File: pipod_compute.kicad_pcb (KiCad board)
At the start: 2 copper layers, 55.5 x 84.8 mm, 2 parts

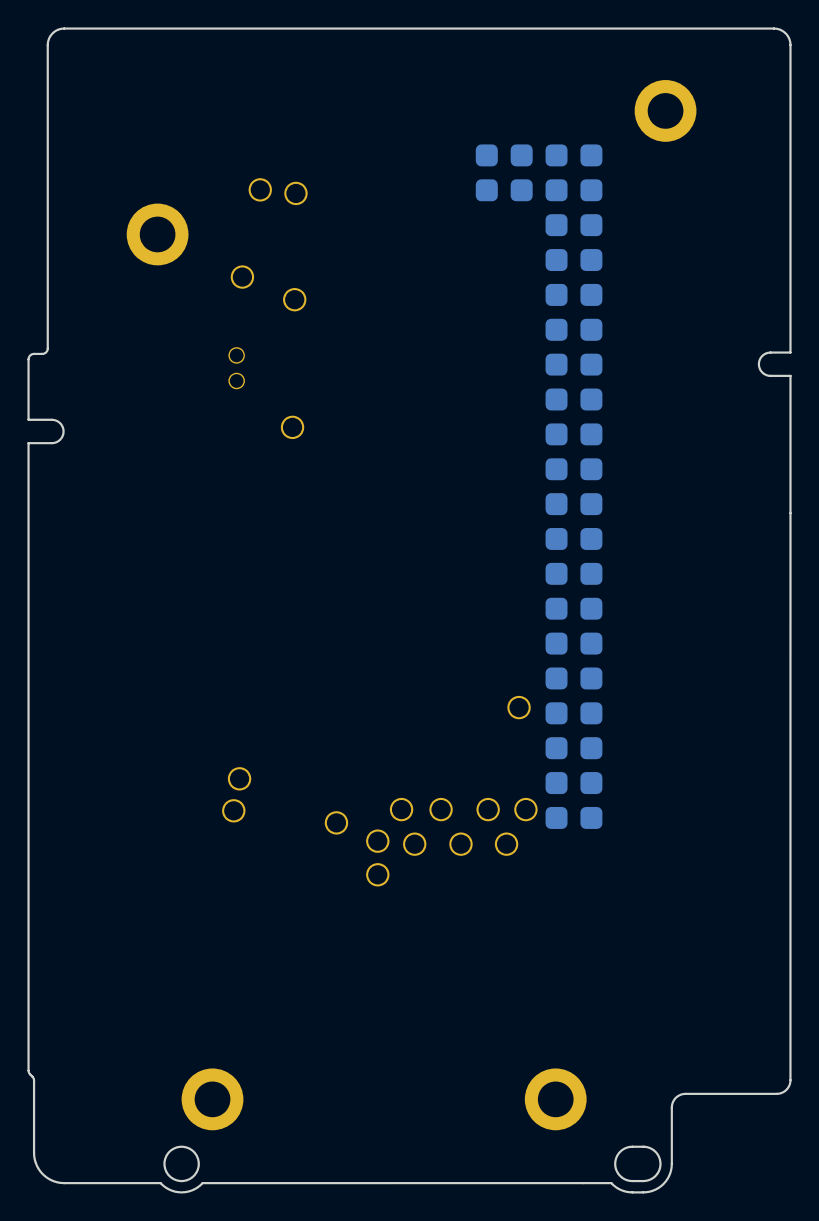
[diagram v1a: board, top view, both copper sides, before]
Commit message: layout: cleanup silkscreen, add bootloader buttons
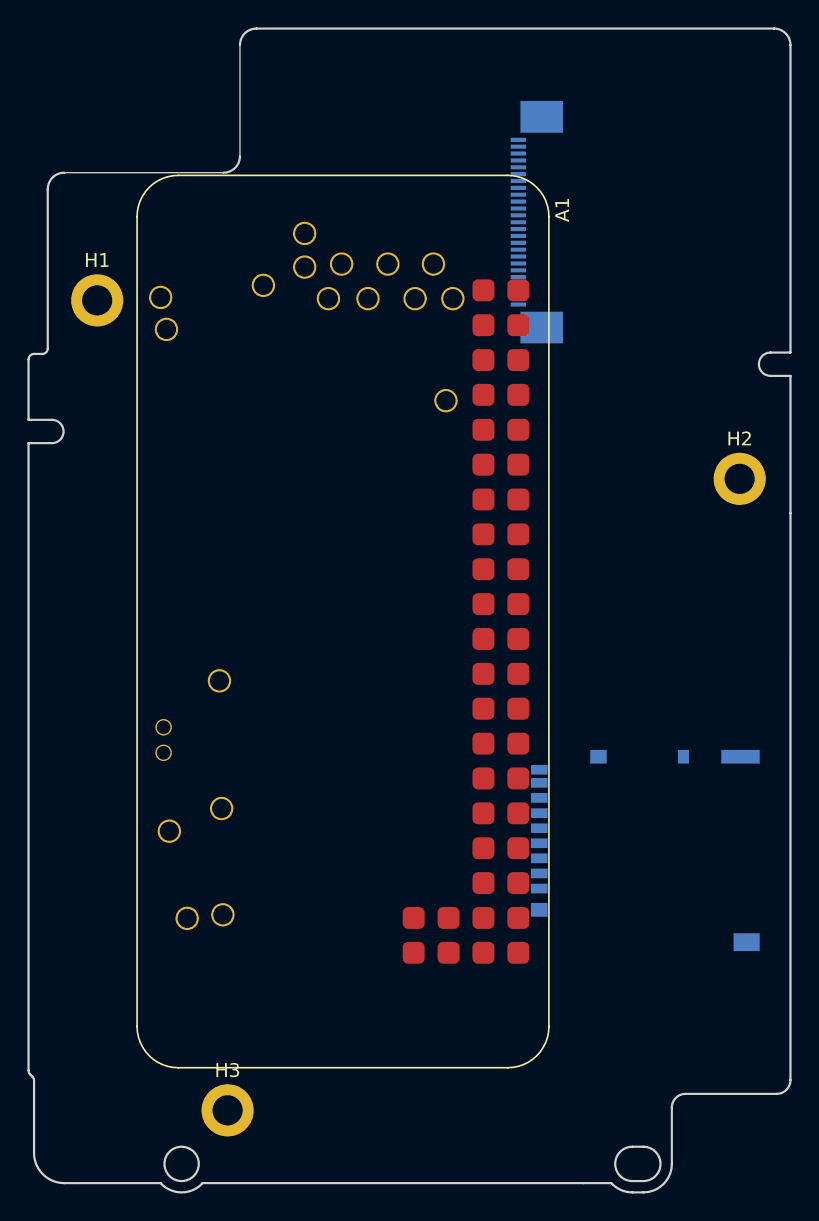
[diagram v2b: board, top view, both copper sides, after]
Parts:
- added H2: MountingHole_Pad, MountingHole:MountingHole_2.2mm_M2_DIN965_Pad, F.Cu at (50.4, 44.8)
- added H3: MountingHole_Pad, MountingHole:MountingHole_2.2mm_M2_DIN965_Pad, F.Cu at (13.1, 90.8)
- added J1: Micro_SD_Card, Gigahawk:microSD_HC_Hirose_DM3AT-SF-PEJM5, B.Cu at (43.5, 71.9)
- added J5: 2-1734839-5, Gigahawk:217348395, B.Cu at (36.8, 26.1)
- A1: moved to F.Cu
- H1: value MountingHole_PiPod -> MountingHole_Pad; footprint pipod_hw:MountingHole_PiPod -> MountingHole:MountingHole_2.2mm_M2_DIN965_Pad
- moved A1 55.4 mm to (36.5, 22.7), turned to -90 degrees
- moved H1 32.0 mm to (3.60, 31.8)
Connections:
- A1 pad PP14: unconnected-(A1-PadPP14) -> SD_CLK
- A1 pad PP15: unconnected-(A1-PadPP15) -> SD_CMD
- A1 pad PP16: unconnected-(A1-PadPP16) -> SD_DAT0
- A1 pad PP17: unconnected-(A1-PadPP17) -> SD_DAT1
- A1 pad PP18: unconnected-(A1-PadPP18) -> SD_DAT2
- A1 pad PP19: unconnected-(A1-PadPP19) -> SD_CD
- A1 pad PP35: unconnected-(A1-PadPP35) -> GND
- A1 pad PP5: unconnected-(A1-PadPP5) -> GND
- A1 pad PP6: unconnected-(A1-PadPP6) -> GND
- H1 pad 1: unconnected-(H1-Pad1) -> GND
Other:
- outline, holes or cut-outs redrawn
- copper layers 2 -> 4

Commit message: compute: finish layout and routing
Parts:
- added C1: 10u, Capacitor_SMD:C_0805_2012Metric, B.Cu at (33.5, 70.2)
- added D1: GRN, LED_SMD:LED_0805_2012Metric, B.Cu at (29.4, 44.7)
- added J2: S7041-42R, Gigahawk:S7041-42R, F.Cu at (44.8, 27.1)
- added J3: S7041-42R, Gigahawk:S7041-42R, F.Cu at (46.2, 73.0)
- added R1: 10k, Resistor_SMD:R_0805_2012Metric, B.Cu at (37.3, 62.9)
- added R2: 470R, Resistor_SMD:R_0805_2012Metric, B.Cu at (27.4, 44.7)
- added TP1: TestPoint, TestPoint:TestPoint_Pad_D1.5mm, B.Cu at (10.2, 80.1)
- added TP10: TestPoint, TestPoint:TestPoint_Pad_D1.5mm, B.Cu at (31.8, 38.1)
- added TP11: TestPoint, TestPoint:TestPoint_Pad_D1.5mm, B.Cu at (21.8, 60.7)
- added TP12: TestPoint, TestPoint:TestPoint_Pad_D1.5mm, B.Cu at (29.1, 57.4)
- added TP13: TestPoint, TestPoint:TestPoint_Pad_D1.5mm, B.Cu at (29.2, 53.9)
- added TP14: TestPoint, TestPoint:TestPoint_Pad_D1.5mm, B.Cu at (42.3, 54.6)
- added TP15: TestPoint, TestPoint:TestPoint_Pad_D1.5mm, B.Cu at (40.5, 56.7)
- added TP16: TestPoint, TestPoint:TestPoint_Pad_D1.5mm, B.Cu at (45.6, 38.6)
- added TP17: TestPoint, TestPoint:TestPoint_Pad_D1.5mm, B.Cu at (48.8, 36.5)
- added TP18: TestPoint, TestPoint:TestPoint_Pad_D1.5mm, B.Cu at (46.3, 34.0)
- added TP19: TestPoint, TestPoint:TestPoint_Pad_D1.5mm, B.Cu at (50.8, 81.3)
- added TP2: TestPoint, TestPoint:TestPoint_Pad_D1.5mm, B.Cu at (46.4, 31.2)
- added TP20: TestPoint, TestPoint:TestPoint_Pad_D1.5mm, B.Cu at (48.3, 81.3)
- added TP21: TestPoint, TestPoint:TestPoint_Pad_D1.5mm, B.Cu at (45.7, 81.3)
- added TP22: TestPoint, TestPoint:TestPoint_Pad_D1.5mm, B.Cu at (43.2, 81.3)
- added TP23: TestPoint, TestPoint:TestPoint_Pad_D1.5mm, B.Cu at (40.6, 81.3)
- added TP24: TestPoint, TestPoint:TestPoint_Pad_D1.5mm, B.Cu at (38.1, 81.3)
- added TP3: TestPoint, TestPoint:TestPoint_Pad_D1.5mm, B.Cu at (28.6, 36.7)
- added TP4: TestPoint, TestPoint:TestPoint_Pad_D1.5mm, B.Cu at (29.5, 41.6)
- added TP5: TestPoint, TestPoint:TestPoint_Pad_D1.5mm, B.Cu at (40.2, 60.8)
- added TP6: TestPoint, TestPoint:TestPoint_Pad_D1.5mm, B.Cu at (37.0, 46.9)
- added TP7: TestPoint, TestPoint:TestPoint_Pad_D1.5mm, B.Cu at (36.4, 40.9)
- added TP8: TestPoint, TestPoint:TestPoint_Pad_D1.5mm, B.Cu at (35.3, 37.9)
- added TP9: TestPoint, TestPoint:TestPoint_Pad_D1.5mm, B.Cu at (29.8, 34.2)
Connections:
- A1 pad 1: unconnected-(A1-Pad1) -> +3V3
- A1 pad 10: unconnected-(A1-Pad10) -> SMC_TX_PI_RX
- A1 pad 11: unconnected-(A1-Pad11) -> Net-(A1-Pad11)
- A1 pad 12: unconnected-(A1-Pad12) -> PI_I2S_BCK
- A1 pad 14: unconnected-(A1-Pad14) -> GND
- A1 pad 16: unconnected-(A1-Pad16) -> SMC_INT
- A1 pad 17: unconnected-(A1-Pad17) -> +3V3
- A1 pad 18: unconnected-(A1-Pad18) -> PI_DISP_DC
- A1 pad 19: unconnected-(A1-Pad19) -> PI_DISP_MOSI
- A1 pad 2: unconnected-(A1-Pad2) -> VCC
- A1 pad 20: unconnected-(A1-Pad20) -> GND
- A1 pad 22: unconnected-(A1-Pad22) -> PI_DISP_RST
- A1 pad 23: unconnected-(A1-Pad23) -> PI_DISP_SCK
- A1 pad 25: unconnected-(A1-Pad25) -> GND
- A1 pad 29: unconnected-(A1-Pad29) -> SD_DET
- A1 pad 3: unconnected-(A1-Pad3) -> SMC_PI_I2C_SDA
- A1 pad 30: unconnected-(A1-Pad30) -> GND
- A1 pad 34: unconnected-(A1-Pad34) -> GND
- A1 pad 35: unconnected-(A1-Pad35) -> PI_I2S_LRCK
- A1 pad 39: unconnected-(A1-Pad39) -> GND
- A1 pad 4: unconnected-(A1-Pad4) -> VCC
- A1 pad 40: unconnected-(A1-Pad40) -> PI_I2S_DIN
- A1 pad 5: unconnected-(A1-Pad5) -> SMC_PI_I2C_SCL
- A1 pad 6: unconnected-(A1-Pad6) -> GND
- A1 pad 8: unconnected-(A1-Pad8) -> SMC_RX_PI_TX
- A1 pad 9: unconnected-(A1-Pad9) -> GND
- A1 pad PP22: unconnected-(A1-PadPP22) -> PI_USB_MUXED_D+
- A1 pad PP23: unconnected-(A1-PadPP23) -> PI_USB_MUXED_D-
- A1 pad PP8: unconnected-(A1-PadPP8) -> +3V3
- A1 pad RUN1: unconnected-(A1-PadRUN1) -> GND
- A1 pad TV1: unconnected-(A1-PadTV1) -> HP_SL_VIDEO
- A1 pad TV2: unconnected-(A1-PadTV2) -> GND
- J1 pad 10: (no net) -> GND
- J1 pad 11: (no net) -> GND
- J1 pad 4: unconnected-(J1-Pad4) -> +3V3
- J1 pad 6: unconnected-(J1-Pad6) -> GND
- J1 pad 9: unconnected-(J1-Pad9) -> SD_DET
- J5 pad 13: SMC_TX_PI_RX -> SMC_RX_PI_TX
- J5 pad 14: SMC_RX_PI_TX -> SMC_TX_PI_RX
- J5 pad 21: PI_VCC -> VCC
- J5 pad 22: PI_VCC -> VCC
- J5 pad 23: PI_VCC -> VCC
- J5 pad 24: PI_VCC -> VCC
- J5 pad 25: PI_VCC -> VCC
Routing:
- net PI_I2S_DIN: track 0.00 -> 73.7 mm, vias 0 -> 1
- net PI_I2S_LRCK: track 0.00 -> 71.7 mm, vias 0 -> 1
- net SD_DAT1: track 0.00 -> 67.8 mm, vias 0 -> 1
- net SD_CLK: track 0.00 -> 63.5 mm, vias 0 -> 1
- net PI_USB_MUXED_D+: track 0.00 -> 63.1 mm
- net PI_USB_MUXED_D-: track 0.00 -> 63.0 mm
- net SD_DAT0: track 0.00 -> 62.8 mm, vias 0 -> 1
- net HP_SL_VIDEO: track 0.00 -> 62.2 mm, vias 0 -> 1
- net SD_CD: track 0.00 -> 61.4 mm, vias 0 -> 2
- net SD_CMD: track 0.00 -> 60.6 mm, vias 0 -> 1
- net SD_DAT2: track 0.00 -> 56.9 mm, vias 0 -> 2
- net +3V3: track 0.00 -> 55.3 mm, vias 0 -> 2
- net GND: track 0.00 -> 54.5 mm, vias 0 -> 23
- net PI_DISP_SCK: track 0.00 -> 49.0 mm, vias 0 -> 2
- net VCC: track 0.00 -> 48.3 mm, vias 0 -> 6
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- added copper zone on In1.Cu, net GND
- added copper zone on In2.Cu, net GND

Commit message: ci: prepare files for CI
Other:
- board text added: "Layers: 4 PCB thickness: 0.8mm Material: FR-4 TG 150-160 Outer Copper: 1oz Inner Copper: 1oz"
- board text added: "PCBWAYPCBWAY"
- board text added: "piPod Compute Board ${TAG} (${REVISION})"
- board text removed: "JLCJLCJLCJLC"
- board text removed: "Layers: 4 PCB thickness: 0.8mm Impedance: Yes (JLC7628)"
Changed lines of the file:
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@@
   (gr_line (start 15.7 98.25) (end 37.1 98.25) (layer "User.2") (width 0.05))
   (gr_line (start 38.6 97.3) (end 38.6 96.5) (layer "User.2") (width 0.05))
-  (gr_text "JLCJLCJLCJLC\n" (at 1.27 66.675 90) (layer "B.SilkS")
+  (gr_text "piPod Compute Board\n${TAG}\n(${REVISION})" (at 23.1 18.1) (layer "F.SilkS")
     (effects (font (size 0.8 0.8) (thickness 0.15)))
   )
-  (gr_text "Layers: 4\nPCB thickness: 0.8mm\nImpedance: Yes (JLC7628)\n" (at 61.39 10.19) (layer "Cmts.User")
+  (gr_text "PCBWAYPCBWAY" (at 21.4 84.4) (layer "F.SilkS")
+    (effects (font (size 0.8 0.8) (thickness 0.15)))
+  )
+  (gr_text "Layers: 4\nPCB thickness: 0.8mm\nMaterial: FR-4 TG 150-160\nOuter Copper: 1oz\nInner Copper: 1oz\n" (at 57.2 31.6) (layer "Cmts.User")
     (effects (font (size 5 5) (thickness 0.5)) (justify left))
   )

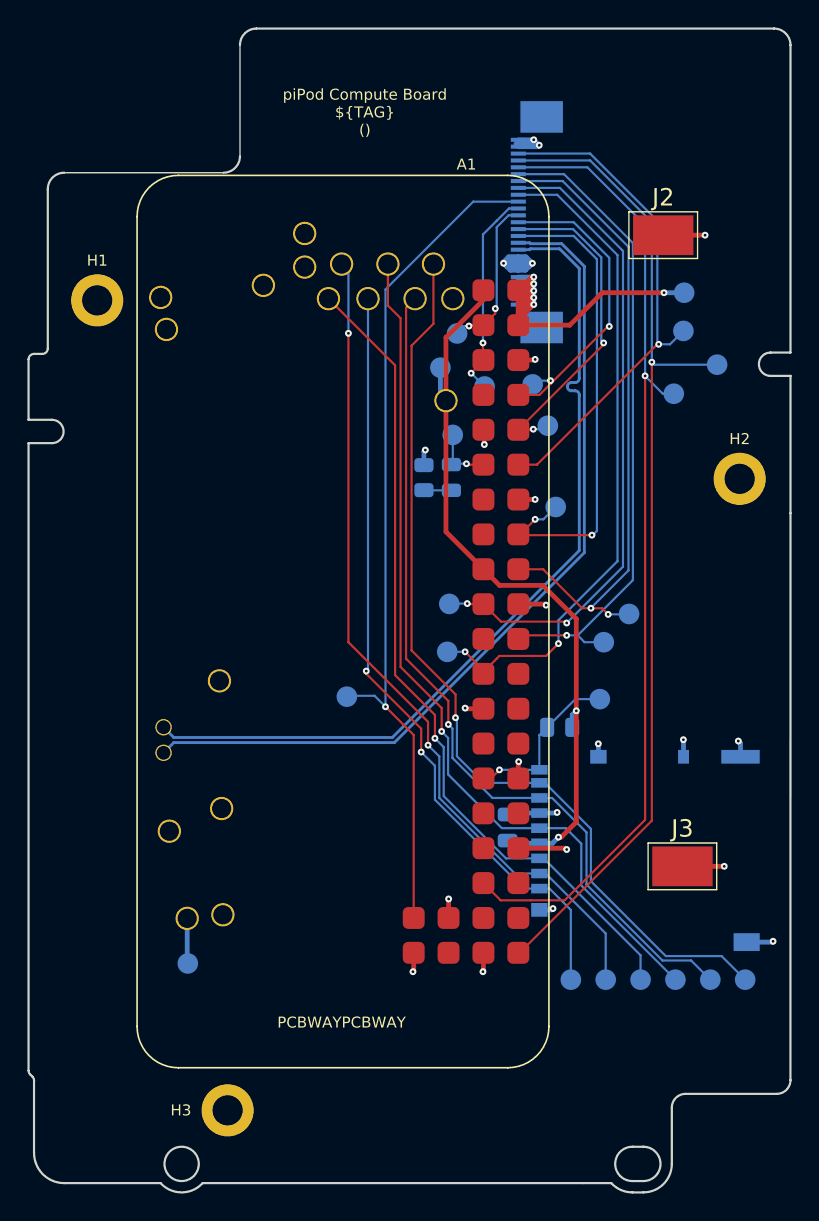
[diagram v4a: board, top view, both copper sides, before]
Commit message: compute: update constraints to match cheaper pcbway tier
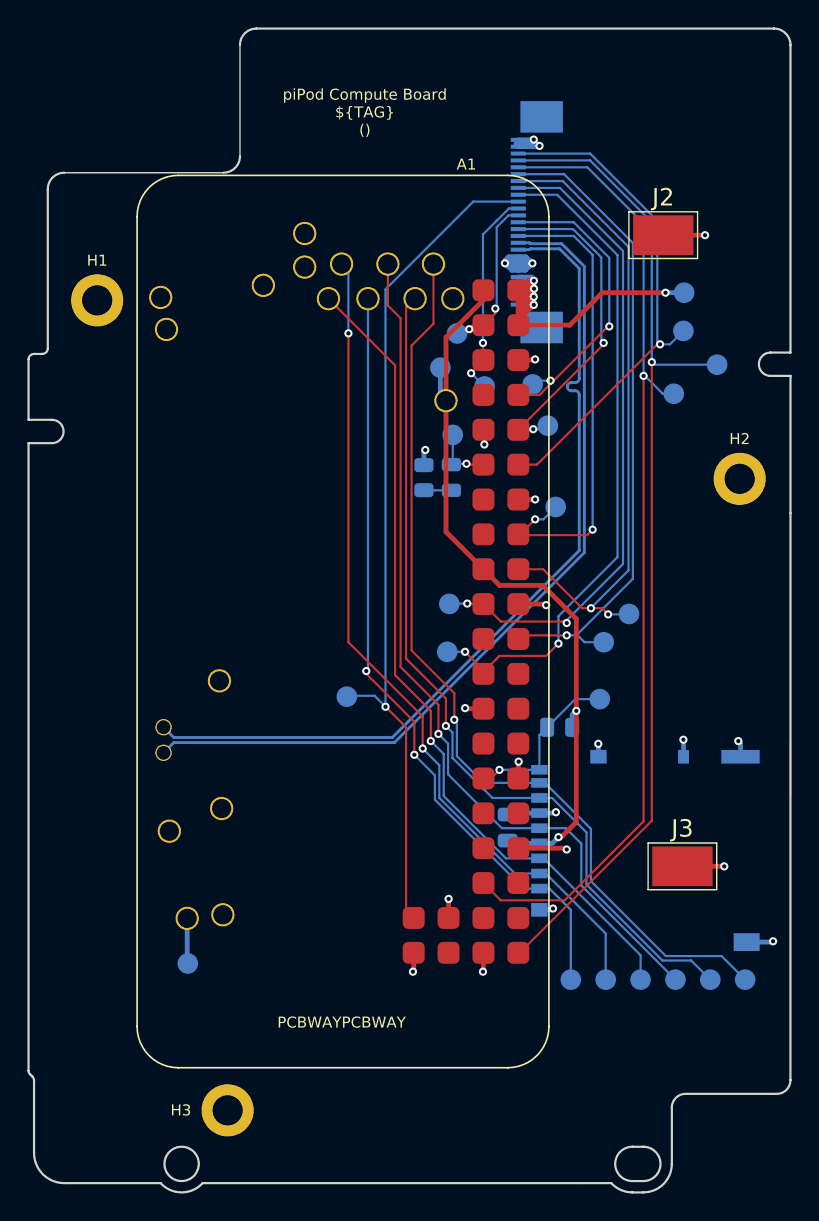
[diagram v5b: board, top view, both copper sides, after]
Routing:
- net VCC: track 48.3 -> 47.5 mm, vias 6 -> 5
- net GND: track 54.5 -> 53.9 mm

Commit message: layout: add OSHW logo, change version text to masked copper
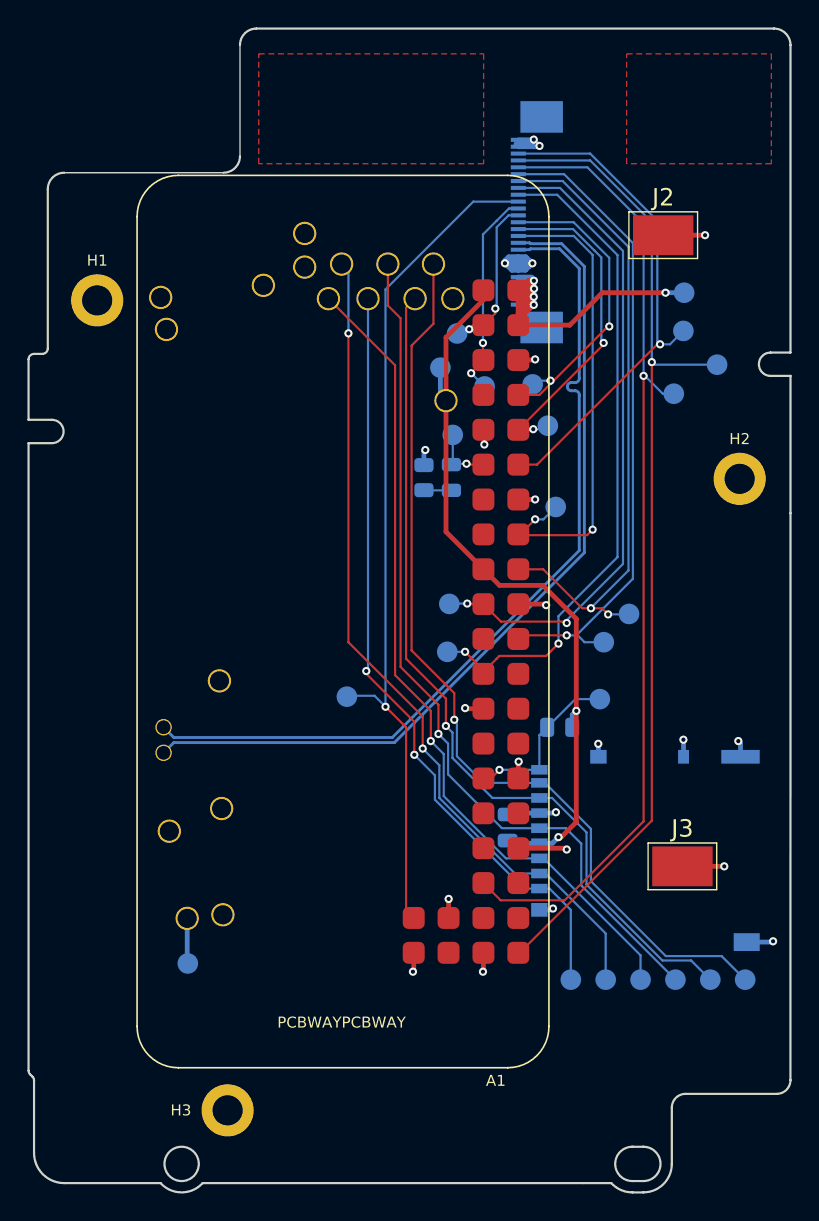
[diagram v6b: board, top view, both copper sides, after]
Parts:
- added LOGO1: Logo_Open_Hardware_Large, Gigahawk:OSHW-Logo2_9.8x8mm_Mask, F.Cu at (47.5, 17.9)
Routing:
- added copper zone on F.Cu, net (none)
